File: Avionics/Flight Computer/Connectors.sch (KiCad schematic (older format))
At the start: 3 parts, among them J1 ERF8-040-05.0-S-DV-K, J2 ERF8-040-05.0-S-DV-K, J3 473460001

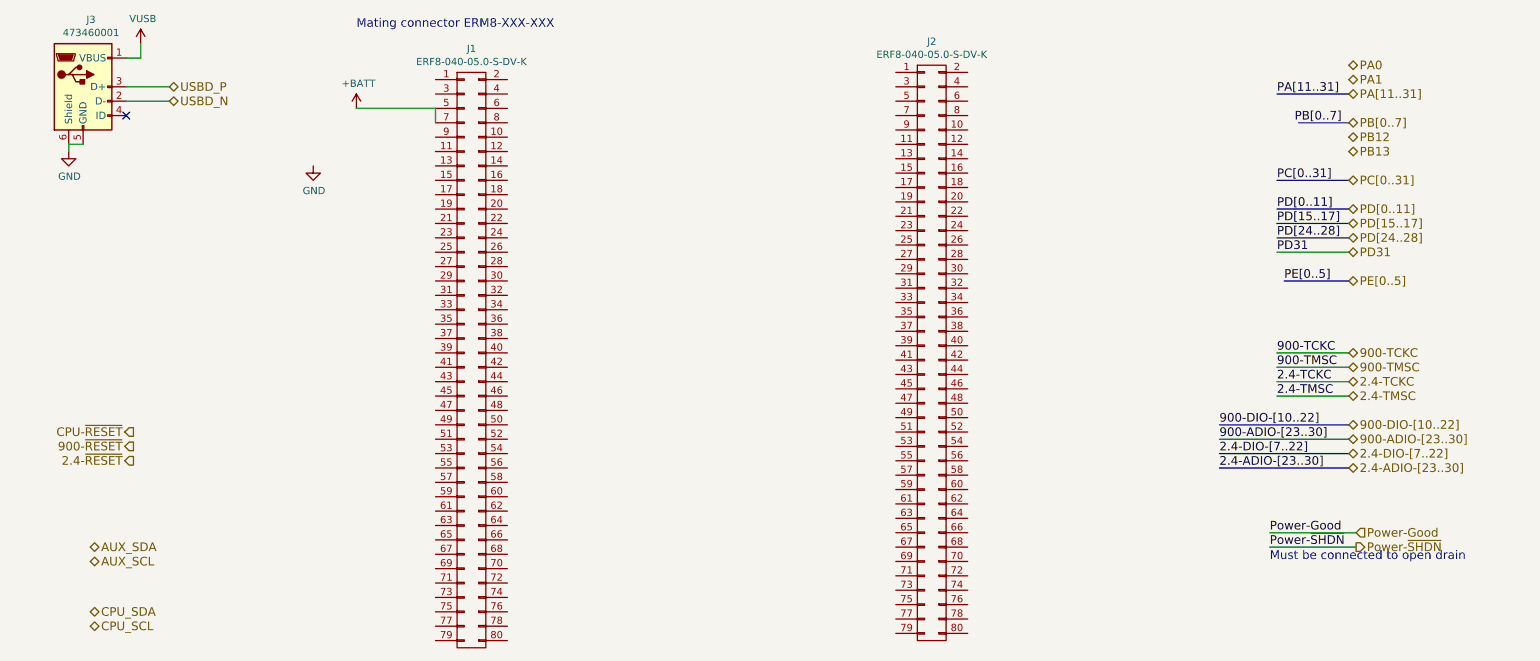
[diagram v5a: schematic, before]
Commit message: Cleaned up vias and DRC Errors
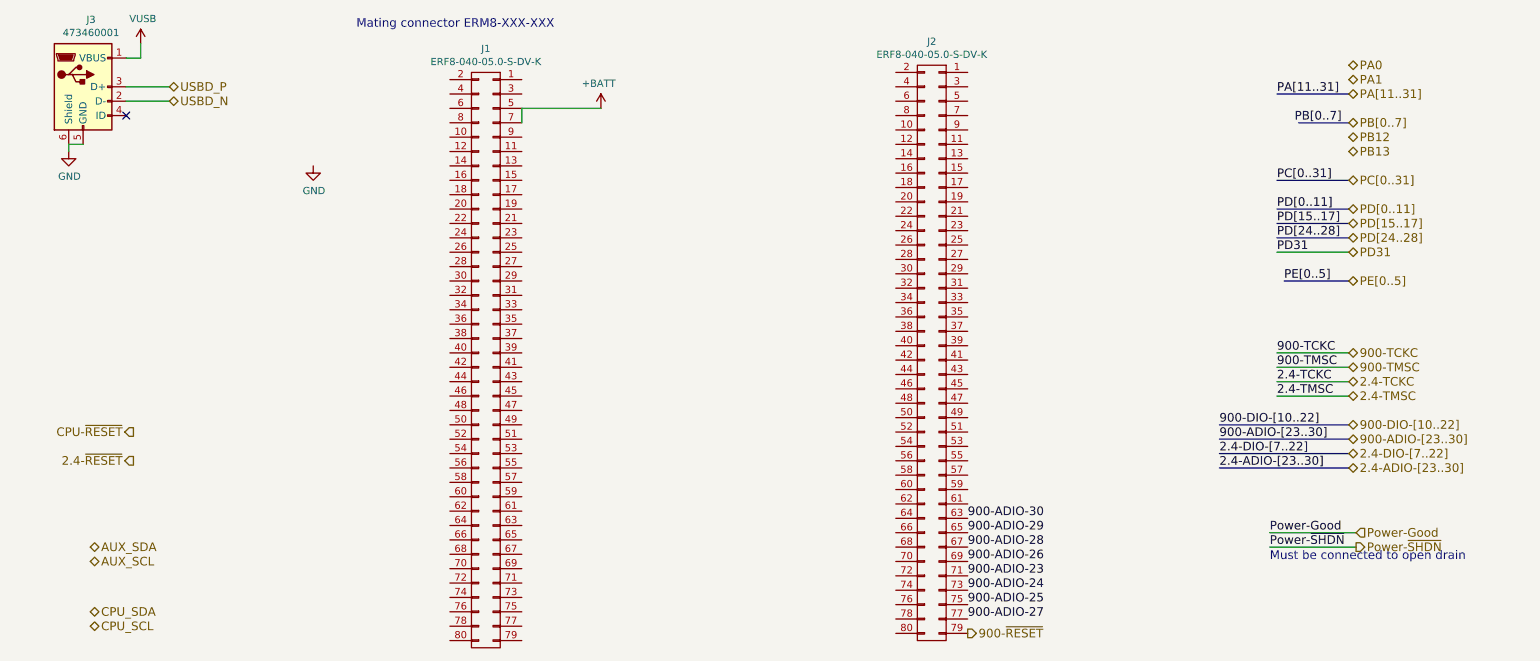
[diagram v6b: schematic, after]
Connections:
- net 900-~RESET: now also J2.79 (P79)
- net 900-ADIO-30: now reaches J2.63 (P63)
- net 900-ADIO-29: now reaches J2.65 (P65)
- net 900-ADIO-28: now reaches J2.67 (P67)
- net 900-ADIO-26: now reaches J2.69 (P69)
- net 900-ADIO-23: now reaches J2.71 (P71)
- net 900-ADIO-24: now reaches J2.73 (P73)
- net 900-ADIO-25: now reaches J2.75 (P75)
- net 900-ADIO-27: now reaches J2.77 (P77)
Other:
- moved on the sheet: J1
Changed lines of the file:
@@
 L CONN_02X40 J1
 U 1 1 58B54687
-P 3900 3350
-F 0 "J1" H 3900 5515 50  0000 C CNN
-F 1 "ERF8-040-05.0-S-DV-K" H 3900 5424 50  0000 C CNN
-F 2 "Connectors_Samtec:ERF8-040-05.0-S-DV-K" H -650 200 50  0001 C CNN
-F 3 "http://suddendocs.samtec.com/prints/erf8-xxx-xx.x-x-dv-xxxx-tr-mkt.pdf" H -650 200 50  0001 C CNN
-	1    3900 3350
-	1    0    0    -1
+P 4000 3350
+F 0 "J1" H 4000 5515 50  0000 C CNN
+F 1 "ERF8-040-05.0-S-DV-K" H 4000 5424 50  0000 C CNN
+F 2 "Connectors_Samtec:ERF8-040-05.0-S-DV-K" H -550 200 50  0001 C CNN
+F 3 "http://suddendocs.samtec.com/prints/erf8-xxx-xx.x-x-dv-xxxx-tr-mkt.pdf" H -550 200 50  0001 C CNN
+	1    4000 3350
+	-1   0    0    -1
 $EndComp
 Text Notes 3100 1050 0    60   ~ 0
@@
 F 3 "http://suddendocs.samtec.com/prints/erf8-xxx-xx.x-x-dv-xxxx-tr-mkt.pdf" H 2550 150 50  0001 C CNN
 	1    7100 3300
-	1    0    0    -1
-$EndComp
-$Comp
-L VUSB #PWR117
+	-1   0    0    -1
+$EndComp
+$Comp
+L VUSB #PWR0116
 U 1 1 58B8BBBA
 P 1600 1150
-F 0 "#PWR117" H -400 -250 50  0001 C CNN
+F 0 "#PWR0116" H -400 -250 50  0001 C CNN
 F 1 "VUSB" H 1615 1323 50  0000 C CNN
 F 2 "" H -400 -100 50  0001 C CNN
@@
 	1600 1250 1600 1150
 $Comp
-L GND #PWR116
+L GND #PWR0117
 U 1 1 58B8BD69
 P 1100 1900
-F 0 "#PWR116" H -800 50  50  0001 C CNN
+F 0 "#PWR0117" H -800 50  50  0001 C CNN
 F 1 "GND" H 1105 1727 50  0000 C CNN
 F 2 "" H -800 300 50  0001 C CNN
@@
 Text HLabel 1550 3850 0    60   Output ~ 0
 CPU-~RESET
-Text HLabel 1550 3950 0    60   Output ~ 0
+Text HLabel 7350 5250 2    60   Output ~ 0
 900-~RESET
 Text HLabel 1550 4050 0    60   Output ~ 0
@@
 Must be connected to open drain\n
 Wire Wire Line
-	3100 1600 3650 1600
-$Comp
-L +BATT #PWR118
+	4800 1600 4250 1600
+$Comp
+L +BATT #PWR0118
 U 1 1 58DB91A4
-P 3100 1600
-F 0 "#PWR118" H 2050 -1300 50  0001 C CNN
-F 1 "+BATT" H 3115 1773 50  0000 C CNN
-F 2 "" H 2050 -1150 50  0001 C CNN
-F 3 "" H 2050 -1150 50  0001 C CNN
-	1    3100 1600
-	1    0    0    -1
-$EndComp
-Wire Wire Line
-	3650 1600 3650 1700
+P 4800 1600
+F 0 "#PWR0118" H 3750 -1300 50  0001 C CNN
+F 1 "+BATT" H 4815 1773 50  0000 C CNN
+F 2 "" H 3750 -1150 50  0001 C CNN
+F 3 "" H 3750 -1150 50  0001 C CNN
+	1    4800 1600
+	-1   0    0    -1
+$EndComp
+Wire Wire Line
+	4250 1600 4250 1700
 Wire Wire Line
 	9500 2600 10000 2600
 $Comp
-L GND #PWR?
+L GND #PWR0119
 U 1 1 58DD26EA
 P 2800 2000
-F 0 "#PWR?" H -1150 -1700 50  0001 C CNN
+F 0 "#PWR0119" H -1150 -1700 50  0001 C CNN
 F 1 "GND" H 2805 1827 50  0000 C CNN
 F 2 "" H -1150 -1450 50  0001 C CNN
@@
 	1    0    0    -1
 $EndComp
+Text Label 7350 4550 0    60   ~ 0
+900-ADIO-29
+Text Label 7350 4450 0    60   ~ 0
+900-ADIO-30
+Text Label 7350 4650 0    60   ~ 0
+900-ADIO-28
+Text Label 7350 4750 0    60   ~ 0
+900-ADIO-26
+Text Label 7350 4950 0    60   ~ 0
+900-ADIO-24
+Text Label 7350 4850 0    60   ~ 0
+900-ADIO-23
+Text Label 7350 5150 0    60   ~ 0
+900-ADIO-27
+Text Label 7350 5050 0    60   ~ 0
+900-ADIO-25
 $EndSCHEMATC

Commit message: Continuing to route out MCU signals.
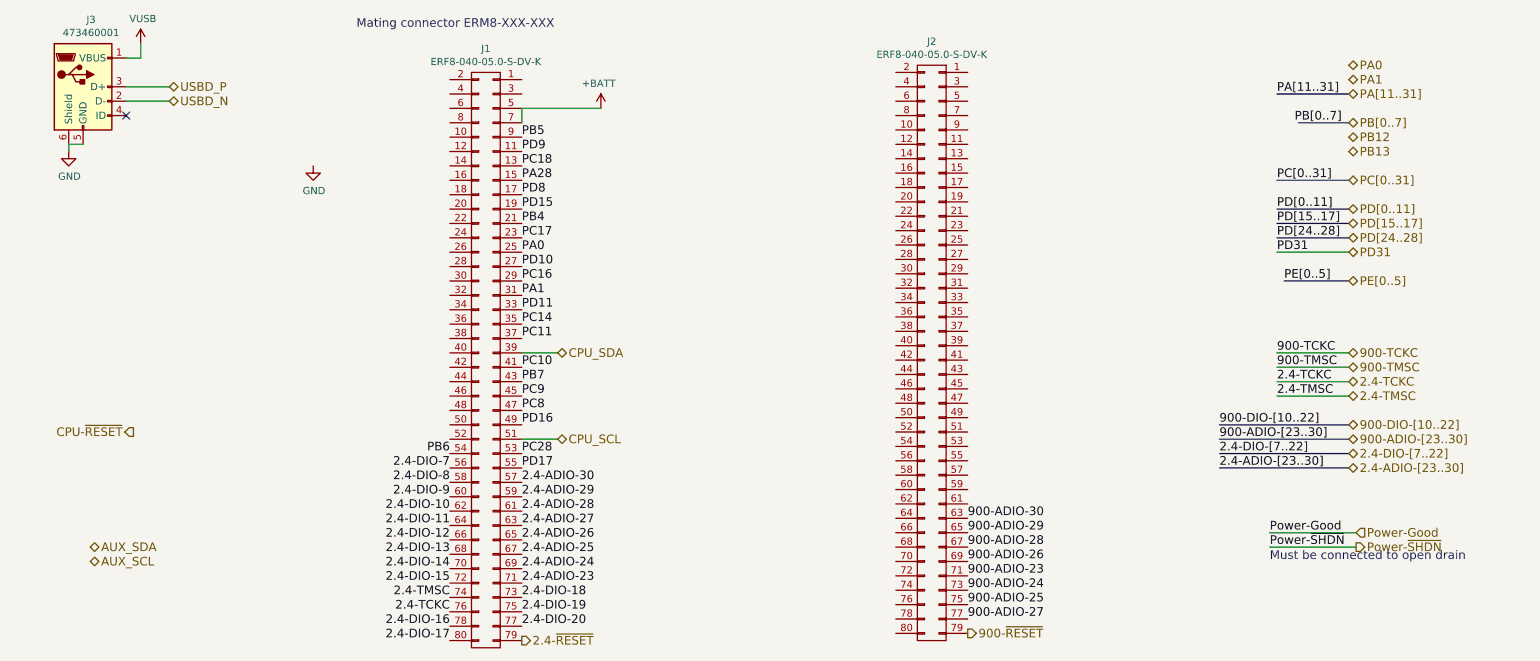
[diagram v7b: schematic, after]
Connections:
- net 2.4-TCKC: now also J1.76 (P76)
- net 2.4-TMSC: now also J1.74 (P74)
- net 2.4-~RESET: now also J1.79 (P79)
- net CPU_SCL: now also J1.51 (P51)
- net CPU_SDA: now also J1.39 (P39)
- net PA0: now also J1.25 (P25)
- net PA1: now also J1.31 (P31)
- net PD9: now reaches J1.11 (P11)
- net PC18: now reaches J1.13 (P13)
- net PA28: now reaches J1.15 (P15)
- net PD8: now reaches J1.17 (P17)
- net PD15: now reaches J1.19 (P19)
- net PB4: now reaches J1.21 (P21)
- net PC17: now reaches J1.23 (P23)
- net PD10: now reaches J1.27 (P27)
- net PC16: now reaches J1.29 (P29)
- net PD11: now reaches J1.33 (P33)
- net PC14: now reaches J1.35 (P35)
- net PC11: now reaches J1.37 (P37)
- net PC10: now reaches J1.41 (P41)
- net PB7: now reaches J1.43 (P43)
- net PC9: now reaches J1.45 (P45)
- net PC8: now reaches J1.47 (P47)
- net PD16: now reaches J1.49 (P49)
- net PC28: now reaches J1.53 (P53)
- net PB6: now reaches J1.54 (P54)
- net PD17: now reaches J1.55 (P55)
- net 2.4-DIO-7: now reaches J1.56 (P56)
- net 2.4-ADIO-30: now reaches J1.57 (P57)
- net 2.4-DIO-8: now reaches J1.58 (P58)
- net 2.4-ADIO-29: now reaches J1.59 (P59)
- net 2.4-DIO-9: now reaches J1.60 (P60)
- net 2.4-ADIO-28: now reaches J1.61 (P61)
- net 2.4-DIO-10: now reaches J1.62 (P62)
- net 2.4-ADIO-27: now reaches J1.63 (P63)
- net 2.4-DIO-11: now reaches J1.64 (P64)
- net 2.4-ADIO-26: now reaches J1.65 (P65)
- net 2.4-DIO-12: now reaches J1.66 (P66)
- net 2.4-ADIO-25: now reaches J1.67 (P67)
- net 2.4-DIO-13: now reaches J1.68 (P68)
- net 2.4-ADIO-24: now reaches J1.69 (P69)
- net 2.4-DIO-14: now reaches J1.70 (P70)
- net 2.4-ADIO-23: now reaches J1.71 (P71)
- net 2.4-DIO-15: now reaches J1.72 (P72)
- net 2.4-DIO-18: now reaches J1.73 (P73)
- net 2.4-DIO-19: now reaches J1.75 (P75)
- net 2.4-DIO-20: now reaches J1.77 (P77)
- net 2.4-DIO-16: now reaches J1.78 (P78)
- net 2.4-DIO-17: now reaches J1.80 (P80)
- net PB5: now reaches J1.9 (P9)
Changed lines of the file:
@@
 Text HLabel 7350 5250 2    60   Output ~ 0
 900-~RESET
-Text HLabel 1550 4050 0    60   Output ~ 0
+Text HLabel 4250 5300 2    60   Output ~ 0
 2.4-~RESET
 Text HLabel 10000 2100 2    60   BiDi ~ 0
@@
 Text HLabel 1250 4750 2    60   BiDi ~ 0
 AUX_SCL
-Text HLabel 1250 5100 2    60   BiDi ~ 0
+Text HLabel 4500 3300 2    60   BiDi ~ 0
 CPU_SDA
-Text HLabel 1250 5200 2    60   BiDi ~ 0
+Text HLabel 4500 3900 2    60   BiDi ~ 0
 CPU_SCL
 Text HLabel 10000 1500 2    60   BiDi ~ 0
@@
 Text Label 7350 5050 0    60   ~ 0
 900-ADIO-25
+Text Label 3750 4200 2    60   ~ 0
+2.4-DIO-8
+Text Label 3750 4300 2    60   ~ 0
+2.4-DIO-9
+Text Label 3750 4400 2    60   ~ 0
+2.4-DIO-10
+Text Label 3750 4500 2    60   ~ 0
+2.4-DIO-11
+Text Label 3750 4600 2    60   ~ 0
+2.4-DIO-12
+Text Label 3750 4700 2    60   ~ 0
+2.4-DIO-13
+Text Label 3750 4800 2    60   ~ 0
+2.4-DIO-14
+Text Label 3750 4900 2    60   ~ 0
+2.4-DIO-15
+Text Label 3750 5100 2    60   ~ 0
+2.4-TCKC
+Text Label 3750 5000 2    60   ~ 0
+2.4-TMSC
+Text Label 3750 5200 2    60   ~ 0
+2.4-DIO-16
+Text Label 3750 5300 2    60   ~ 0
+2.4-DIO-17
+Text Label 4250 5000 0    60   ~ 0
+2.4-DIO-18
+Text Label 4250 5100 0    60   ~ 0
+2.4-DIO-19
+Text Label 4250 5200 0    60   ~ 0
+2.4-DIO-20
+Text Label 4250 4900 0    60   ~ 0
+2.4-ADIO-23
+Text Label 4250 4800 0    60   ~ 0
+2.4-ADIO-24
+Text Label 4250 4700 0    60   ~ 0
+2.4-ADIO-25
+Text Label 4250 4600 0    60   ~ 0
+2.4-ADIO-26
+Text Label 4250 4500 0    60   ~ 0
+2.4-ADIO-27
+Text Label 4250 4400 0    60   ~ 0
+2.4-ADIO-28
+Text Label 4250 4300 0    60   ~ 0
+2.4-ADIO-29
+Text Label 4250 4200 0    60   ~ 0
+2.4-ADIO-30
+Text Label 4250 4100 0    60   ~ 0
+PD17
+Text Label 4250 4000 0    60   ~ 0
+PC28
+Wire Wire Line
+	4250 3900 4500 3900
+Text Label 4250 3800 0    60   ~ 0
+PD16
+Text Label 4250 3700 0    60   ~ 0
+PC8
+Text Label 4250 3600 0    60   ~ 0
+PC9
+Text Label 4250 3500 0    60   ~ 0
+PB7
+Text Label 4250 3400 0    60   ~ 0
+PC10
+Wire Wire Line
+	4500 3300 4250 3300
+Text Label 4250 3100 0    60   ~ 0
+PC14
+Text Label 4250 3000 0    60   ~ 0
+PD11
+Text Label 4250 2900 0    60   ~ 0
+PA1
+Text Label 4250 2800 0    60   ~ 0
+PC16
+Text Label 4250 2700 0    60   ~ 0
+PD10
+Text Label 4250 2600 0    60   ~ 0
+PA0
+Text Label 4250 2500 0    60   ~ 0
+PC17
+Text Label 4250 2400 0    60   ~ 0
+PB4
+Text Label 4250 2300 0    60   ~ 0
+PD15
+Text Label 3750 4100 2    60   ~ 0
+2.4-DIO-7
+Text Label 3750 4000 2    60   ~ 0
+PB6
+Text Label 4250 3200 0    60   ~ 0
+PC11
+Text Label 4250 2200 0    60   ~ 0
+PD8
+Text Label 4250 2100 0    60   ~ 0
+PA28
+Text Label 4250 2000 0    60   ~ 0
+PC18
+Text Label 4250 1900 0    60   ~ 0
+PD9
+Text Label 4250 1800 0    60   ~ 0
+PB5
 $EndSCHEMATC

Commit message: Did some more routing
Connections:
- net 900-ADIO-23: now also J2.77 (P77); no longer J2.71 (P71)
- net 900-ADIO-24: now also J2.75 (P75); no longer J2.73 (P73)
- net 900-ADIO-25: now also J2.73 (P73); no longer J2.75 (P75)
- net 900-ADIO-26: now also J2.71 (P71); no longer J2.69 (P69)
- net 900-ADIO-27: now also J2.69 (P69); no longer J2.77 (P77)
- net PC19: now reaches J1.1 (P1)
- net PA31: now reaches J1.10 (P10)
- net PC21: now reaches J1.2 (P2)
- net PA30: now reaches J1.3 (P3)
- net PD6: now reaches J1.4 (P4)
- net PC20: now reaches J1.6 (P6)
- net PD7: now reaches J1.8 (P8)
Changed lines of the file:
@@
 Text Label 7350 4650 0    60   ~ 0
 900-ADIO-28
+Text Label 7350 4850 0    60   ~ 0
+900-ADIO-26
+Text Label 7350 5050 0    60   ~ 0
+900-ADIO-24
+Text Label 7350 5150 0    60   ~ 0
+900-ADIO-23
 Text Label 7350 4750 0    60   ~ 0
-900-ADIO-26
+900-ADIO-27
 Text Label 7350 4950 0    60   ~ 0
-900-ADIO-24
-Text Label 7350 4850 0    60   ~ 0
-900-ADIO-23
-Text Label 7350 5150 0    60   ~ 0
-900-ADIO-27
-Text Label 7350 5050 0    60   ~ 0
 900-ADIO-25
 Text Label 3750 4200 2    60   ~ 0
@@
 Text Label 4250 1800 0    60   ~ 0
 PB5
+Text Label 4250 1500 0    60   ~ 0
+PA30
+Text Label 4250 1400 0    60   ~ 0
+PC19
+Text Label 3750 1800 2    60   ~ 0
+PA31
+Text Label 3750 1700 2    60   ~ 0
+PD7
+Text Label 3750 1600 2    60   ~ 0
+PC20
+Text Label 3750 1500 2    60   ~ 0
+PD6
+Text Label 3750 1400 2    60   ~ 0
+PC21
 $EndSCHEMATC
